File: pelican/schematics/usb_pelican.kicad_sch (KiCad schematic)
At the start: 7 parts

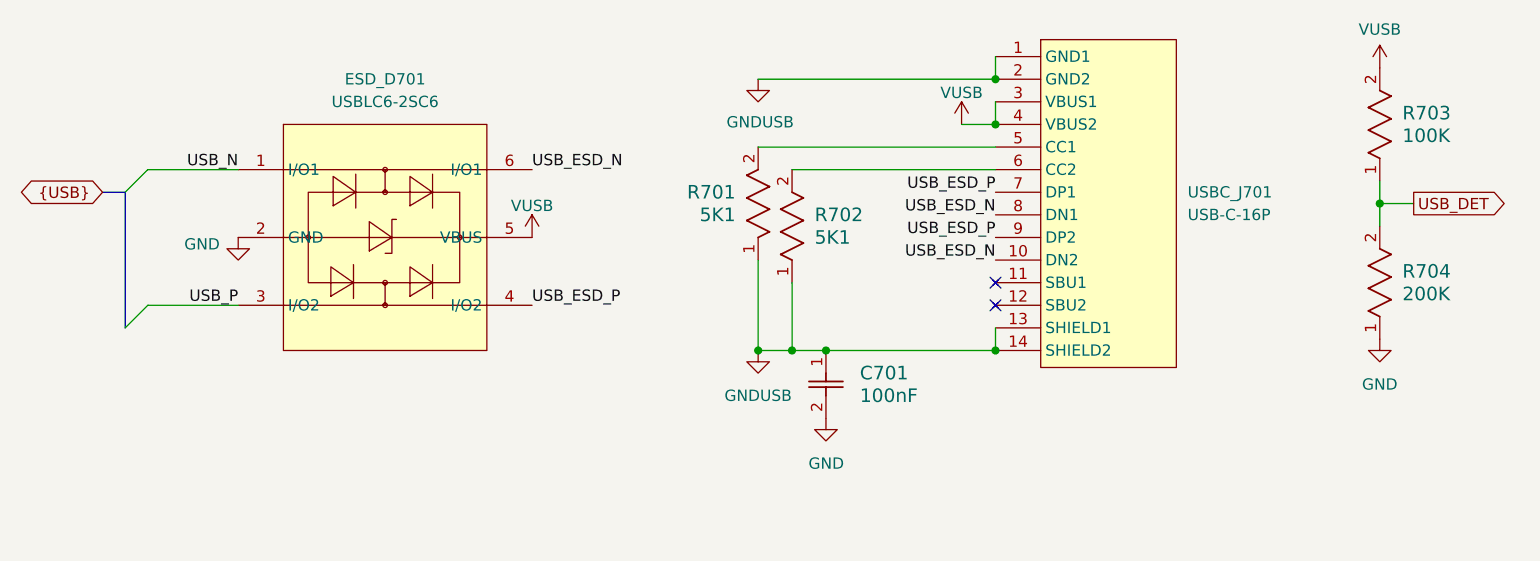
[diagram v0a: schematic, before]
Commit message: Update Pelican design libraries and save connector layout concept
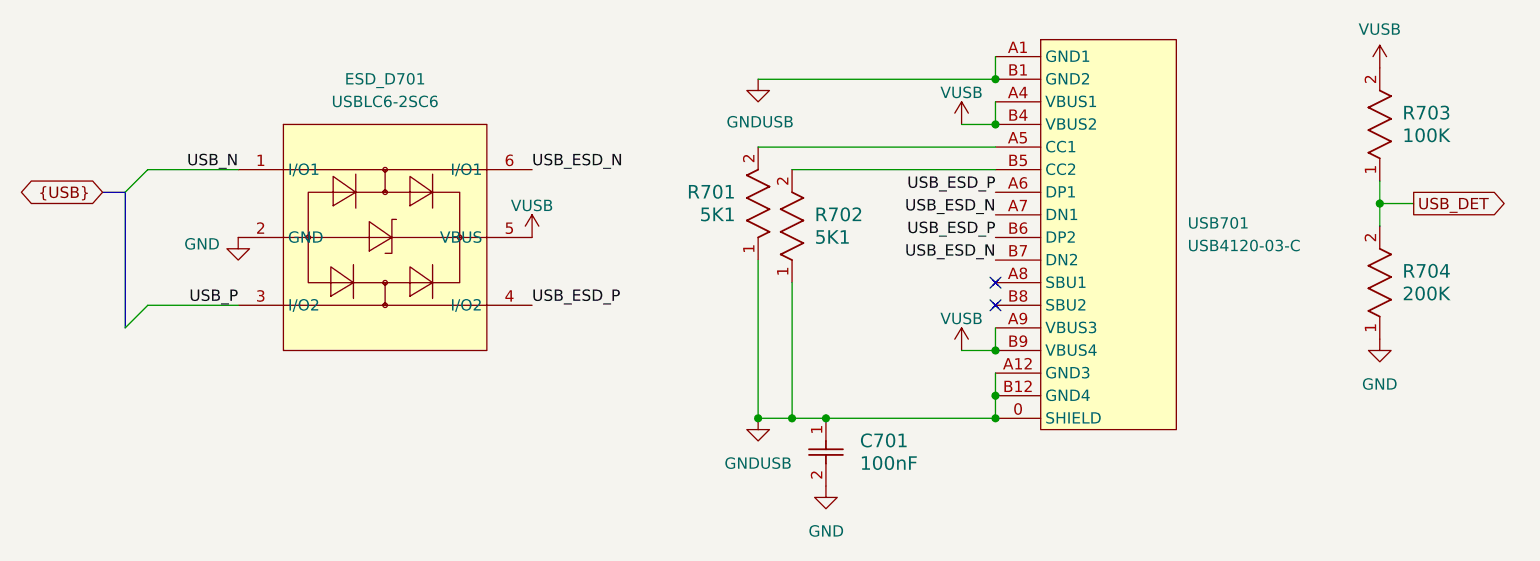
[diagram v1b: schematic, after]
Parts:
- removed USBC_J701: USB-C-16P, J_USB-C-16P:J_USB-C-16P_SMD, symbol J_USB-C-16P:USB-C-16P
- added USB701: USB4120-03-C, J_USB4120-03-C:J_USB4120-03-C_SMD, symbol J_USB4120-03-C:USB4120-03-C
- C701: LCSC Part # C71629 -> C1525
- R701, R702: LCSC Part # C105872 -> C25905
- R703: LCSC Part # C60491 -> C25741
- R704: LCSC Part # C114763 -> C25764
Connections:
- net GNDUSB: now also USB701.0 (SHIELD), USB701.A1 (GND1), USB701.A12 (GND3), USB701.B1 (GND2), USB701.B12 (GND4)
- net USB_ESD_N: now also USB701.A7 (DN1), USB701.B7 (DN2)
- net USB_ESD_P: now also USB701.A6 (DP1), USB701.B6 (DP2)
- net VUSB: now also USB701.A4 (VBUS1), USB701.A9 (VBUS3), USB701.B4 (VBUS2), USB701.B9 (VBUS4)
- net at R702.2: now also USB701.B5 (CC2)
- net at R701.2: now also USB701.A5 (CC1)
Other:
- moved on the sheet: C701
